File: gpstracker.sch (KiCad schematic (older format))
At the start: 53 parts, among them IC1 SIM808, J2 Leds, J3 47553-0001, J4 CONN_COAXIAL, J5 CONN_COAXIAL, J6 Micro_SD_Card, Q1 DMP1045U, SW1 Reset, U1 MCP73832-5-OT, U2 ATMEGA328P-AU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

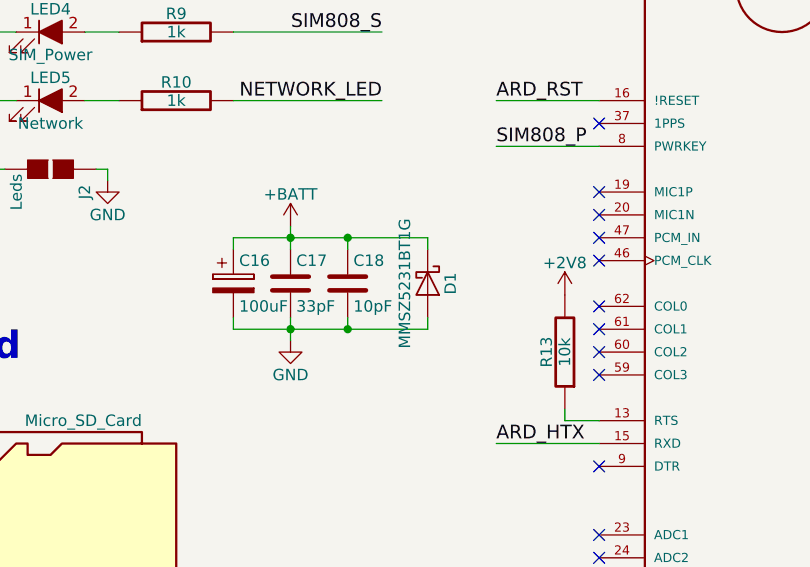
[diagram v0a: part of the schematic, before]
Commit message: Updated schematics references with updated and available parts. This is the version that was ordered on Mouser/Seeedstudio
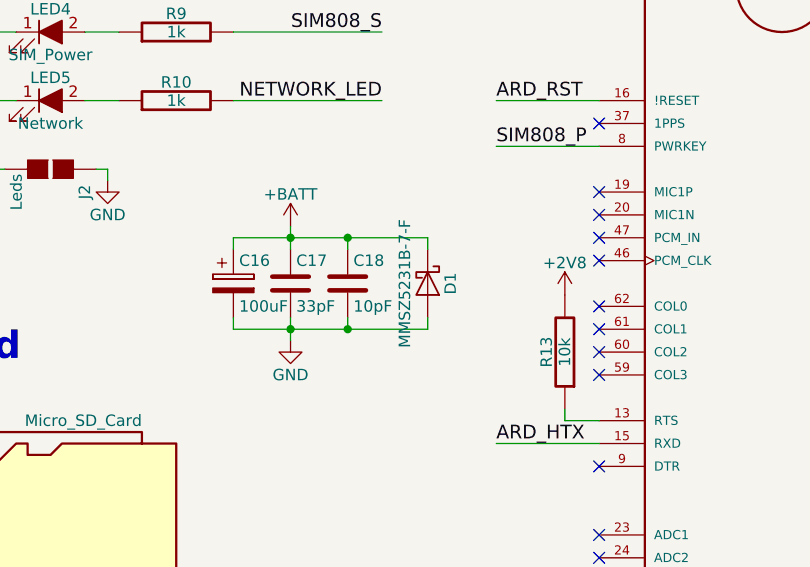
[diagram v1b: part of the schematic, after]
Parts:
- C17: Manufacturer Kemet -> Vishay; Manufacturer part number C0805C330K4HACAUTO -> VJ0805A330GXJCW1BC
- C18: Manufacturer Kemet -> Vishay; Manufacturer part number C0805C100K4HACAUTO -> VJ0805A100GXJCW1BC
- D1: value MMSZ5231BT1G -> MMSZ5231B-7-F; Manufacturer ON Semiconductor -> Diodes Incorporated; Manufacturer part number MMSZ5231BT1G -> MMSZ5231B-7-F
- LED5: Package (none) -> 0805
- R14, R15: Manufacturer part number ERJ-6GEYJ513V -> ERJ-6ENF5102V
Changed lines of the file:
@@
 F 4 "Kingbright" H 6400 1550 60  0001 C CNN "Manufacturer"
 F 5 "APT2012EC" H 6400 1550 60  0001 C CNN "Manufacturer part number"
+F 6 "0805" H 6400 1550 60  0001 C CNN "Package"
 	1    6400 1550
 	1    0    0    -1
@@
 F 3 "" H 4750 2950 60  0000 C CNN
 F 4 "Panasonic" V 4750 2950 60  0001 C CNN "Manufacturer"
-F 5 "ERJ-6GEYJ513V" V 4750 2950 60  0001 C CNN "Manufacturer part number"
+F 5 "ERJ-6ENF5102V" V 4750 2950 60  0001 C CNN "Manufacturer part number"
 F 6 "0805" V 4750 2950 60  0001 C CNN "Package"
 	1    4750 2950
@@
 F 3 "" H 4950 2950 60  0000 C CNN
 F 4 "Panasonic" V 4950 2950 60  0001 C CNN "Manufacturer"
-F 5 "ERJ-6GEYJ513V" V 4950 2950 60  0001 C CNN "Manufacturer part number"
+F 5 "ERJ-6ENF5102V" V 4950 2950 60  0001 C CNN "Manufacturer part number"
 F 6 "0805" V 4950 2950 60  0001 C CNN "Package"
 	1    4950 2950
@@
 F 2 "Capacitors_SMD:C_0805_HandSoldering" H 7488 2200 50  0001 C CNN
 F 3 "" H 7450 2350 50  0001 C CNN
-F 4 "Kemet" H 7450 2350 60  0001 C CNN "Manufacturer"
-F 5 "C0805C330K4HACAUTO" H 7450 2350 60  0001 C CNN "Manufacturer part number"
+F 4 "Vishay" H 7450 2350 60  0001 C CNN "Manufacturer"
+F 5 "VJ0805A330GXJCW1BC" H 7450 2350 60  0001 C CNN "Manufacturer part number"
 F 6 "0805" H 7450 2350 60  0001 C CNN "Package"
 	1    7450 2350
@@
 F 2 "Capacitors_SMD:C_0805_HandSoldering" H 7738 2200 50  0001 C CNN
 F 3 "" H 7700 2350 50  0001 C CNN
-F 4 "Kemet" H 7700 2350 60  0001 C CNN "Manufacturer"
-F 5 "C0805C100K4HACAUTO" H 7700 2350 60  0001 C CNN "Manufacturer part number"
+F 4 "Vishay" H 7700 2350 60  0001 C CNN "Manufacturer"
+F 5 "VJ0805A100GXJCW1BC" H 7700 2350 60  0001 C CNN "Manufacturer part number"
 F 6 "0805" H 7700 2350 60  0001 C CNN "Package"
 	1    7700 2350
@@
 P 8050 2350
 F 0 "D1" H 8050 2450 50  0000 C CNN
-F 1 "MMSZ5231BT1G" H 8050 2250 50  0000 C CNN
+F 1 "MMSZ5231B-7-F" H 8050 2250 50  0000 C CNN
 F 2 "Diodes_SMD:D_SOD-123" H 8050 2350 50  0001 C CNN
 F 3 "" H 8050 2350 50  0001 C CNN
-F 4 "ON Semiconductor" H 8050 2350 60  0001 C CNN "Manufacturer"
-F 5 "MMSZ5231BT1G" H 8050 2350 60  0001 C CNN "Manufacturer part number"
+F 4 "Diodes Incorporated" H 8050 2350 60  0001 C CNN "Manufacturer"
+F 5 "MMSZ5231B-7-F" H 8050 2350 60  0001 C CNN "Manufacturer part number"
 F 6 "SOD-123-2" H 8050 2350 60  0001 C CNN "Package"
 	1    8050 2350

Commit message: Augmented the pad size of the battery holder for hand soldering
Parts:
- BT2: footprint Battery_Holders:Keystone_1058_1x2032-CoinCell -> custom-conn:Keystone_1058_1x2032-CoinCell
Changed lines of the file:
@@
 F 0 "BT2" H 6500 7550 50  0000 L CNN
 F 1 "Backup battery" H 6500 7450 50  0000 L CNN
-F 2 "Battery_Holders:Keystone_1058_1x2032-CoinCell" V 6400 7510 50  0001 C CNN
+F 2 "custom-conn:Keystone_1058_1x2032-CoinCell" V 6400 7510 50  0001 C CNN
 F 3 "" V 6400 7510 50  0001 C CNN
 F 4 "Keystone" H 6400 7450 60  0001 C CNN "Manufacturer"

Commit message: Replaced MOLEX_104031-0811 with cheaper and easier Hirose_DM3AT-SF-PEJM5
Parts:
- J6: footprint 104031-0811:MOLEX_104031-0811 -> Connectors_Card:Hirose_DM3AT-SF-PEJM5
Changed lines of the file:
@@
 F 0 "J6" H 5500 4150 50  0000 C CNN
 F 1 "Micro_SD_Card" H 6800 4150 50  0000 R CNN
-F 2 "104031-0811:MOLEX_104031-0811" H 7300 3850 50  0001 C CNN
+F 2 "Connectors_Card:Hirose_DM3AT-SF-PEJM5" H 7300 3850 50  0001 C CNN
 F 3 "" H 6150 3550 50  0001 C CNN
 F 4 "Molex" H 6150 3550 60  0001 C CNN "Manufacturer"

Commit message: Fix SIM808 reset pin being tied to hardware reset. Fixed ground pads on sdcard
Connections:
- net ARD_HRX: now also U2.11 ((PCINT23/AIN1)PD7); no longer U2.10 ((PCINT22/OC0A/AIN0)PD6)
- net ARD_HTX: now also U2.10 ((PCINT22/OC0A/AIN0)PD6); no longer U2.9 ((PCINT21/OC0B/T1)PD5)
- net ARD_RST: no longer IC1.16 (!RESET)
- net GND: no longer J6.9 (SHIELD)
- new net SIM_RST: IC1.16 (!RESET), U2.9 ((PCINT21/OC0B/T1)PD5)
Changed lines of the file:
@@
 NoConn ~ 3050 3900
 Text Label 3500 5400 2    60   ~ 0
-ARD_HRX
+ARD_HTX
 Text Label 3500 5300 2    60   ~ 0
-ARD_HTX
+SIM_RST
 Text Label 3500 3300 2    60   ~ 0
 SIM808_P
@@
 NoConn ~ 3050 4250
 NoConn ~ 3050 4350
-NoConn ~ 3050 5500
 NoConn ~ 1150 4550
 NoConn ~ 1150 4650
@@
 NoConn ~ 8800 2750
 Text Label 8350 1550 0    60   ~ 0
-ARD_RST
+SIM_RST
 NoConn ~ 8800 1650
 Text Label 8350 1750 0    60   ~ 0
@@
 	5250 3350 4250 3350
 Wire Wire Line
-	6950 4150 7000 4150
-Wire Wire Line
-	7000 4150 7000 4350
-Wire Wire Line
-	7000 4350 5100 4350
-Connection ~ 5100 4350
-Wire Wire Line
 	3050 5000 3500 5000
 Wire Wire Line
@@
 	-1   0    0    1
 $EndComp
+Wire Wire Line
+	3050 5500 3500 5500
+Text Label 3500 5500 2    60   ~ 0
+ARD_HRX
+NoConn ~ 6950 4150
 $EndSCHEMATC

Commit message: Pulled down WP pin of 24LC512 to avoid floating pin issues that prevents writing to the chip (not reported on pcb yet).
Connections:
- net GND: now also U3.7 (WP)
- no-connect marks 48 -> 47
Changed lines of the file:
@@
 	0    1    1    0
 $EndComp
-NoConn ~ 4400 7300
 Text Label 3300 4550 2    60   ~ 0
 SCL
@@
 ARD_HRX
 NoConn ~ 6950 4150
+$Comp
+L GND #PWR?
+U 1 1 5A78E6A2
+P 4450 7350
+F 0 "#PWR?" H 4450 7100 50  0001 C CNN
+F 1 "GND" H 4450 7200 50  0000 C CNN
+F 2 "" H 4450 7350 50  0001 C CNN
+F 3 "" H 4450 7350 50  0001 C CNN
+	1    4450 7350
+	1    0    0    -1
+$EndComp
+Wire Wire Line
+	4450 7350 4450 7300
+Wire Wire Line
+	4450 7300 4400 7300
 $EndSCHEMATC

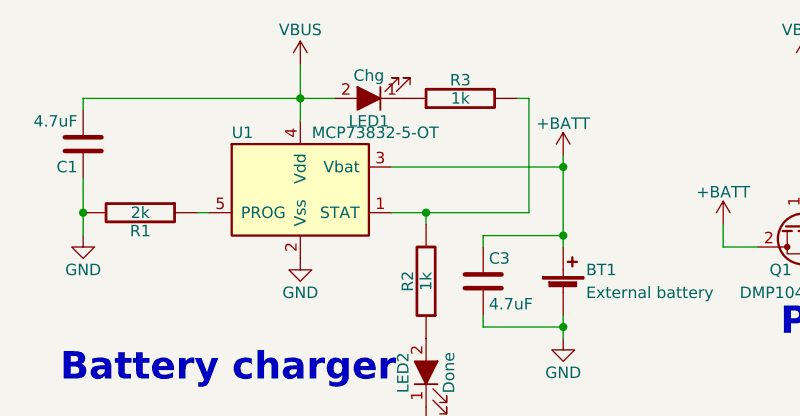
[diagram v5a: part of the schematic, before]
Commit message: Changed MCP73831T-2ACI/OT to MCP73832T-5ACI/OT
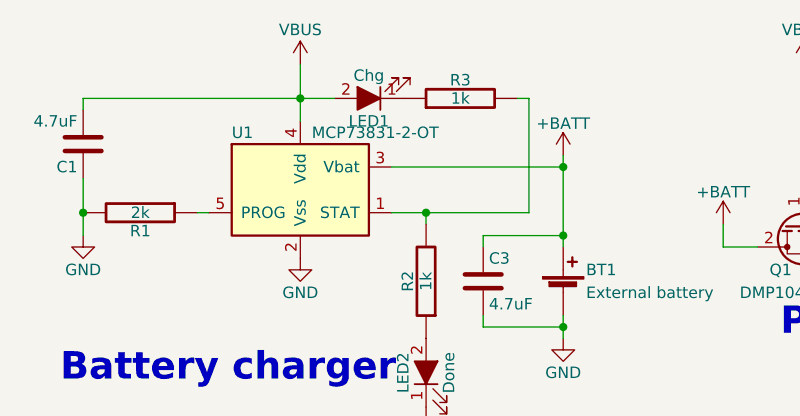
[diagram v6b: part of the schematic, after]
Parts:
- U1: value MCP73832-5-OT -> MCP73831-2-OT; Manufacturer part number MCP73832T-5ACI/OT -> MCP73831T-2ACI/OT
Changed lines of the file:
@@
 P 1600 1300
 F 0 "U1" H 1300 1550 50  0000 L CNN
-F 1 "MCP73832-5-OT" H 1650 1550 50  0000 L CNN
+F 1 "MCP73831-2-OT" H 1650 1550 50  0000 L CNN
 F 2 "TO_SOT_Packages_SMD:SOT-23-5_HandSoldering" H 1650 1050 50  0001 L CIN
 F 3 "" H 1450 1250 50  0001 C CNN
 F 4 "Microchip" H 1600 1300 60  0001 C CNN "Manufacturer"
-F 5 "MCP73832T-5ACI/OT" H 1600 1300 60  0001 C CNN "Manufacturer part number"
+F 5 "MCP73831T-2ACI/OT" H 1600 1300 60  0001 C CNN "Manufacturer part number"
 F 6 "SOT-23" H 1600 1300 60  0001 C CNN "Package"
 	1    1600 1300

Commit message: Reported last changes from schematics to PCB
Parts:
- J6: Manufacturer Molex -> Hirose; Manufacturer part number 104031-0811 -> DM3AT-SF-PEJM5
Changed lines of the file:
@@
 F 2 "Connectors_Card:Hirose_DM3AT-SF-PEJM5" H 7300 3850 50  0001 C CNN
 F 3 "" H 6150 3550 50  0001 C CNN
-F 4 "Molex" H 6150 3550 60  0001 C CNN "Manufacturer"
-F 5 "104031-0811" H 6150 3550 60  0001 C CNN "Manufacturer part number"
+F 4 "Hirose" H 6150 3550 60  0001 C CNN "Manufacturer"
+F 5 "DM3AT-SF-PEJM5" H 6150 3550 60  0001 C CNN "Manufacturer part number"
 	1    6150 3550
 	1    0    0    -1
